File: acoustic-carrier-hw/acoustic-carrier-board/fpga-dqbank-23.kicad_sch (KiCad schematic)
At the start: 0 parts

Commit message: [carrier] Added hierarchical labels
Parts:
- added C15, C5, C58, C59: 10nF, Capacitor_SMD:C_0402_1005Metric, symbol Device:C_Small
- added C17, C18, C33, C36, C49, C57: 0.1uF, Capacitor_SMD:C_0402_1005Metric, symbol Device:C_Small
- added C41: 4.7uF, Capacitor_SMD:C_0402_1005Metric, symbol Device:C_Small
- added C6: 10uF, Capacitor_SMD:C_0603_1608Metric, symbol Device:C_Small
- added IC1: ECP5-BGA256, iw-fpga_mcu:BGA256C80P16X16_1400X1400X170, symbol iw-fpga_mcu:ECP5-BGA256
- added L11: 120@100MHz, Inductor_SMD:L_0603_1608Metric, symbol Device:L_Small
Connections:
- new net CLK: IC1.P15 (PR32B/RDQSN32)
- new net D0: IC1.R16 (PR35B/VREF1_3)
- new net D1: IC1.M13 (PR35C)
- new net D2: IC1.N14 (PR35D/RDQ32)
- new net D3: IC1.N13 (PR38A/RDQ44)
- new net D4: IC1.P14 (PR38B)
- new net D5: IC1.R15 (PR38C)
- new net D6: IC1.T15 (PR38D)
- new net D7: IC1.P13 (PR41A)
- new net DIR: IC1.M14 (PR32D)
- new net DQ0: IC1.B16 (PR2A/RDQ8)
- new net DQ1: IC1.B15 (PR2B/S0_IN)
- new net DQ10: IC1.J12 (PR17D)
- new net DQ11: IC1.J14 (PR20C/GR_PCLK2_1)
- new net DQ12: IC1.K14 (PR20D/GR_PCLK2_0)
- new net DQ13: IC1.J16 (PR23A/PCLKT2_1)
- new net DQ14: IC1.J15 (PR23B/PCLKC2_1)
- new net DQ15: IC1.K16 (PR23C/PCLKT2_0)
- new net DQ2: IC1.C14 (PR2C)
- new net DQ3: IC1.D14 (PR2D)
- new net DQ4: IC1.C16 (PR5A)
- new net DQ5: IC1.C15 (PR5B)
- new net DQ6: IC1.E14 (PR5C)
- new net DQ7: IC1.F14 (PR5D)
- new net DQ8: IC1.H13 (PR17B)
- new net DQ9: IC1.J13 (PR17C)
- new net FPGA_CC1: IC1.R13 (PR41C)
- new net FPGA_CC2: IC1.T14 (PR41D)
- new net FPGA_USB_SENSE: IC1.R12 (PR44A/RDQS44)
- new net GND: C15.2, C17.2, C18.2, C33.2, C36.2, C41.2, C49.2, C5.2, C57.2, C58.2, C59.2, C6.2
- new net LDM: IC1.F13 (PR8C)
- new net LDQS: IC1.D16 (PR8A/RDQS8)
- new net LDQS#: IC1.E15 (PR8B/RDQSN8)
- new net NXT: IC1.P16 (PR35A)
- new net RST: IC1.N16 (PR32A/RDQS32)
- new net STP: IC1.L14 (PR32C)
- new net UDM: IC1.K15 (PR23D/PCLKC2_0/RDQ20)
- new net UDQS: IC1.G16 (PR20A/RDQS20)
- new net UDQS#: IC1.H15 (PR20B/RDQSN20)
- new net VCORE_3V3: C33.1, C36.1, C41.1, IC1.K11 (VCCIO3_1), IC1.L11 (VCCIO3_2)
- new net VDDR3L_1.35: L11.2
- new net VDDR_BANK: C49.1, C57.1, C58.1, C59.1, C6.1, IC1.H11 (VCCIO2_1), IC1.J11 (VCCIO2_2), L11.1
- new net VDRR3L_0.675: C15.1, C17.1, C18.1, C5.1, IC1.G14 (PR14C/VREF1_2)
- no-connect marks 0 -> 25

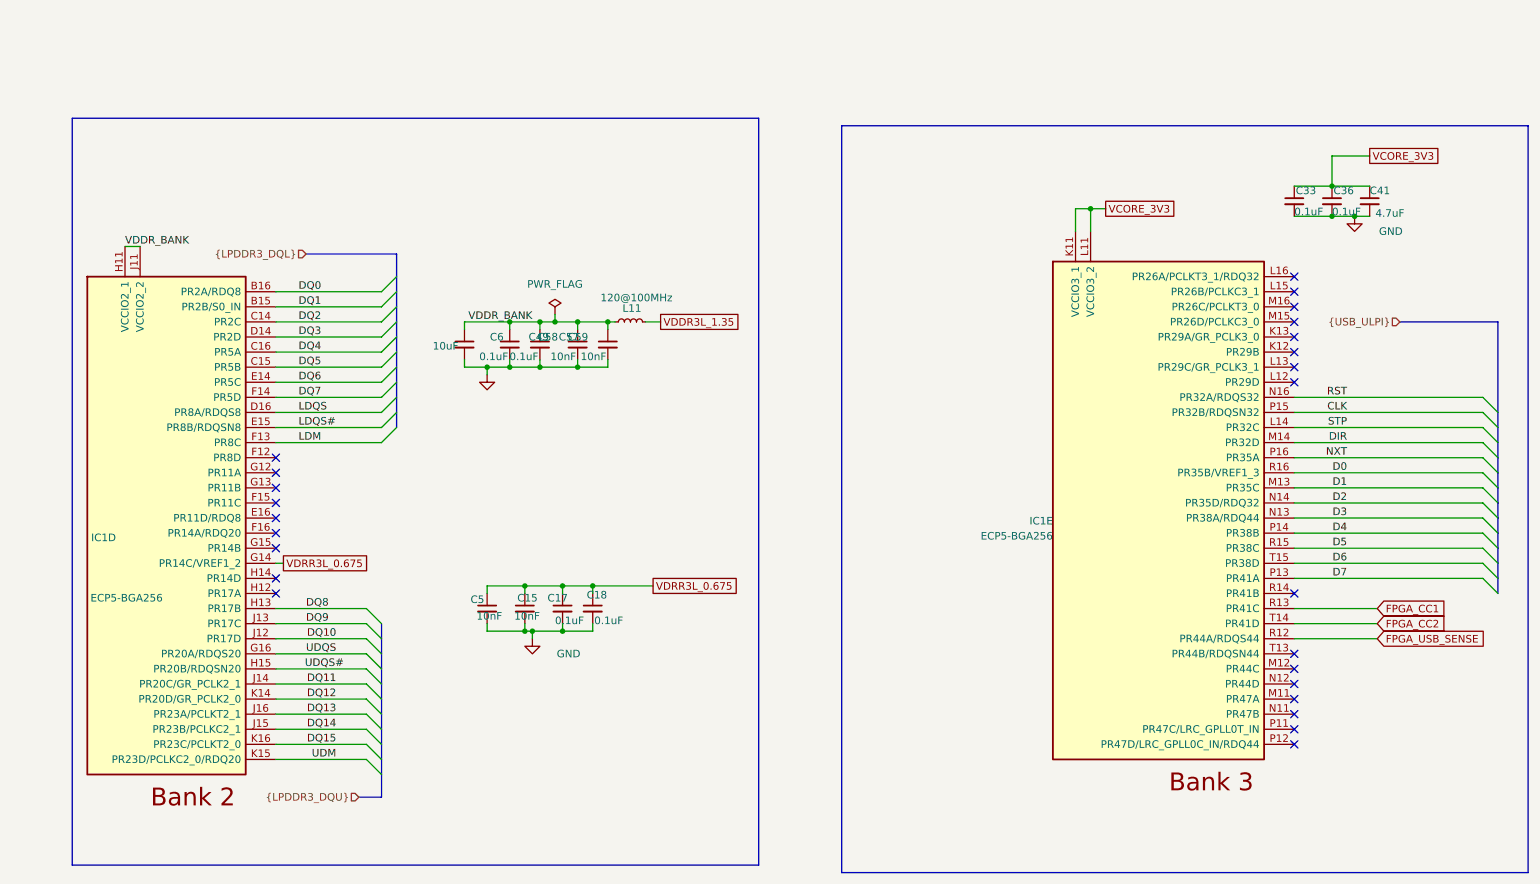
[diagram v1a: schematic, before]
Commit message: [carrier] Added decoupling caps to flash and comparators
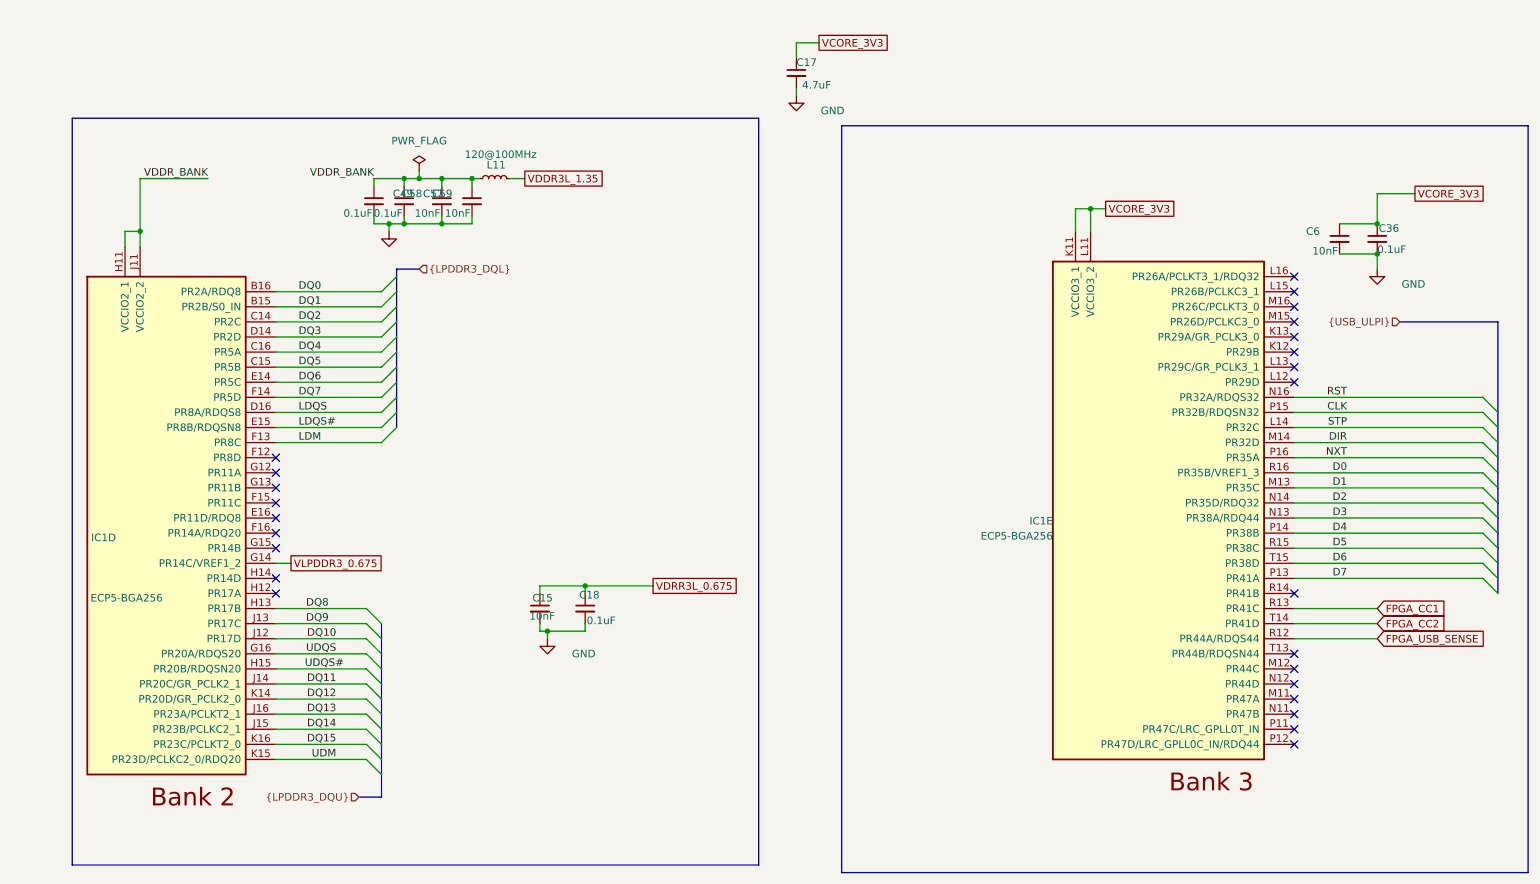
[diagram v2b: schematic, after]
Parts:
- removed C33: 0.1uF, Capacitor_SMD:C_0402_1005Metric, symbol Device:C_Small
- removed C41: 4.7uF, Capacitor_SMD:C_0402_1005Metric, symbol Device:C_Small
- removed C5: 10nF, Capacitor_SMD:C_0402_1005Metric, symbol Device:C_Small
- C17: value 0.1uF -> 4.7uF; LPN C307331 -> C23733; MPN CL05B104KB54PNC -> CL05A475MP5NRNC
- C6: value 10uF -> 10nF; footprint Capacitor_SMD:C_0603_1608Metric -> Capacitor_SMD:C_0402_1005Metric; LPN C19702 -> CL05B103KB5NNNC; MPN CL10A106KP8NNNC -> C15195
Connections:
- net VCORE_3V3: now also C17.1, C6.1
- net VDDR_BANK: no longer C6.1
- net VDRR3L_0.675: no longer C17.1, IC1.G14 (PR14C/VREF1_2)
- new net VLPDDR3_0.675: IC1.G14 (PR14C/VREF1_2)
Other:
- moved on the sheet: C15, C18, C36, C49, C57, C58, C59, L11

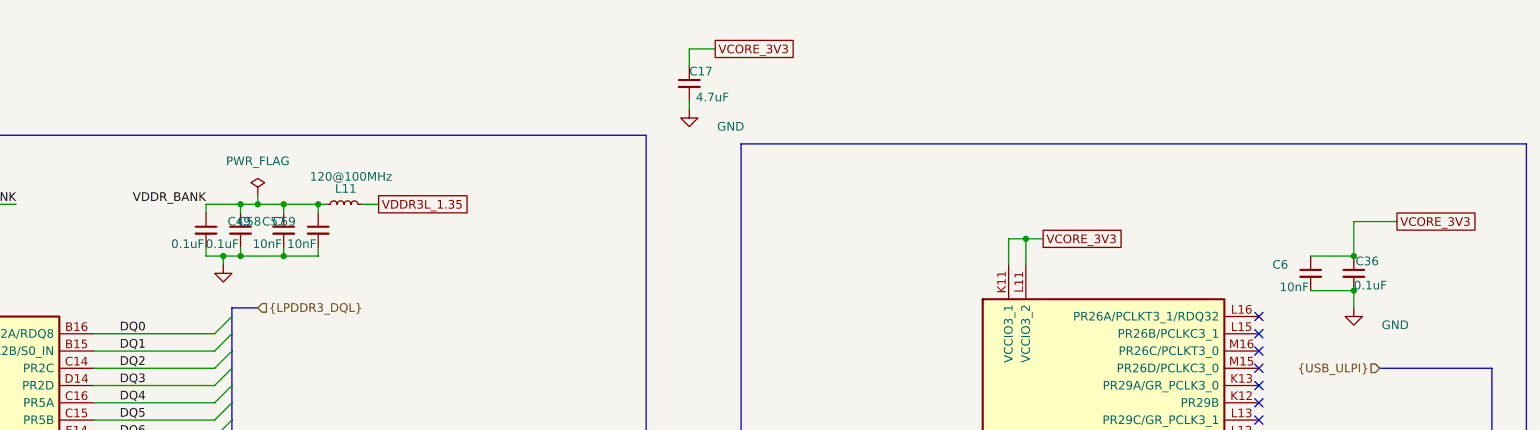
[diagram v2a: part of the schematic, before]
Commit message: [carrier] Added extra decoupling to ECP5U according to datasheet (next) perform page-wise checks, add testpoints
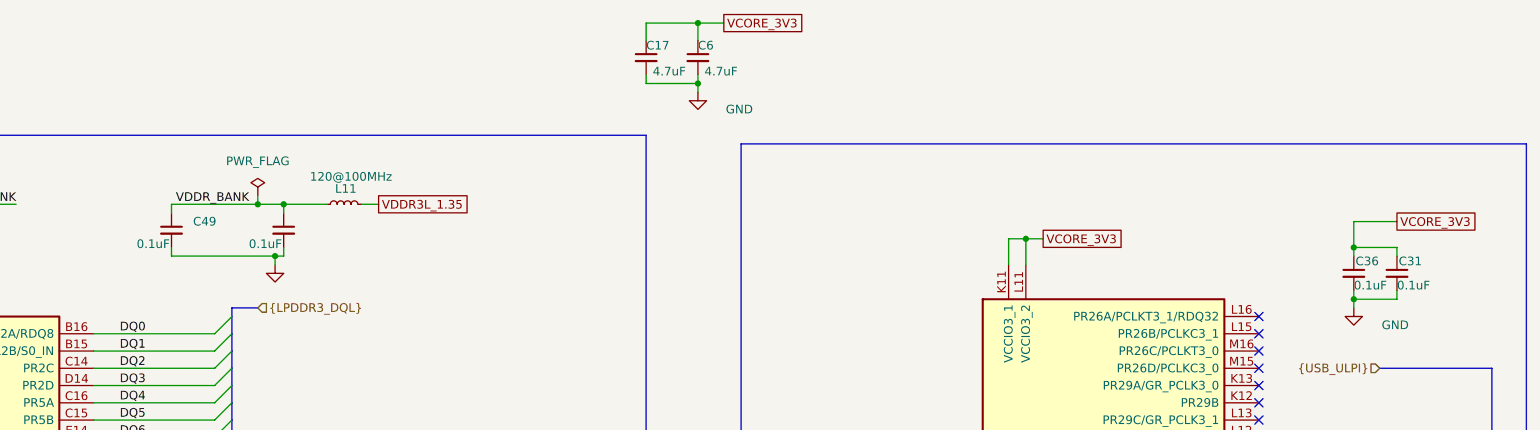
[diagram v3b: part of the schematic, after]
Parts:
- removed C58, C59: 10nF, Capacitor_SMD:C_0402_1005Metric, symbol Device:C_Small
- added C31: 0.1uF, Capacitor_SMD:C_0402_1005Metric, symbol Device:C_Small
- C6: value 10nF -> 4.7uF; LPN CL05B103KB5NNNC -> C23733; MPN C15195 -> CL05A475MP5NRNC
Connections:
- net GND: now also C31.2
- net VCORE_3V3: now also C31.1
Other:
- moved on the sheet: C49

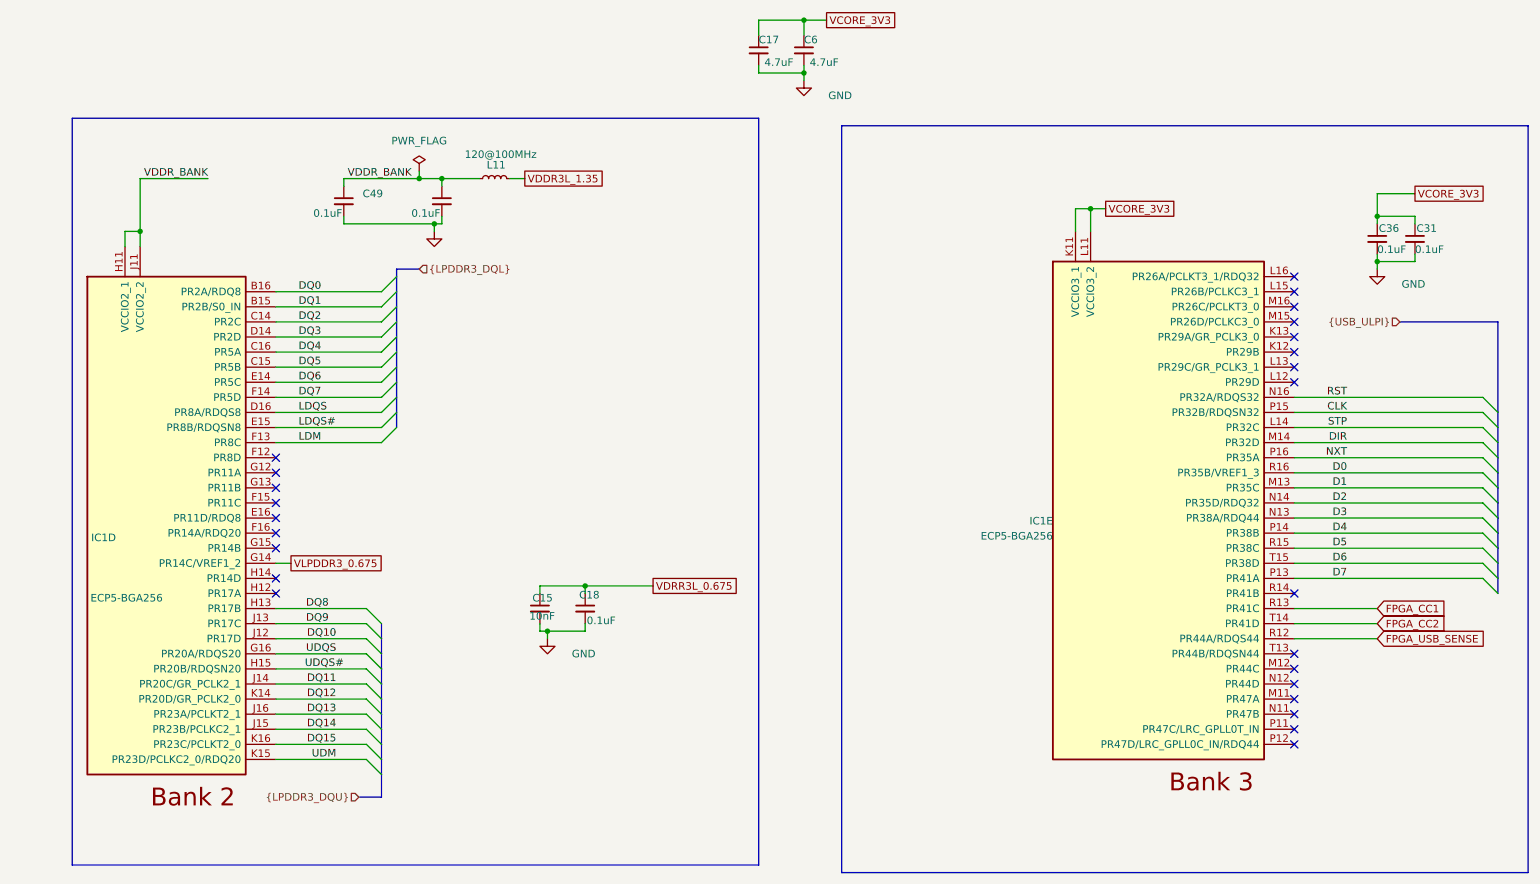
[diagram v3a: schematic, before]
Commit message: [¢arrier] Did major cchecks of ETH, DDR, ANALOG, config (next) check buffer circuit driven by USB-CC, then start layout
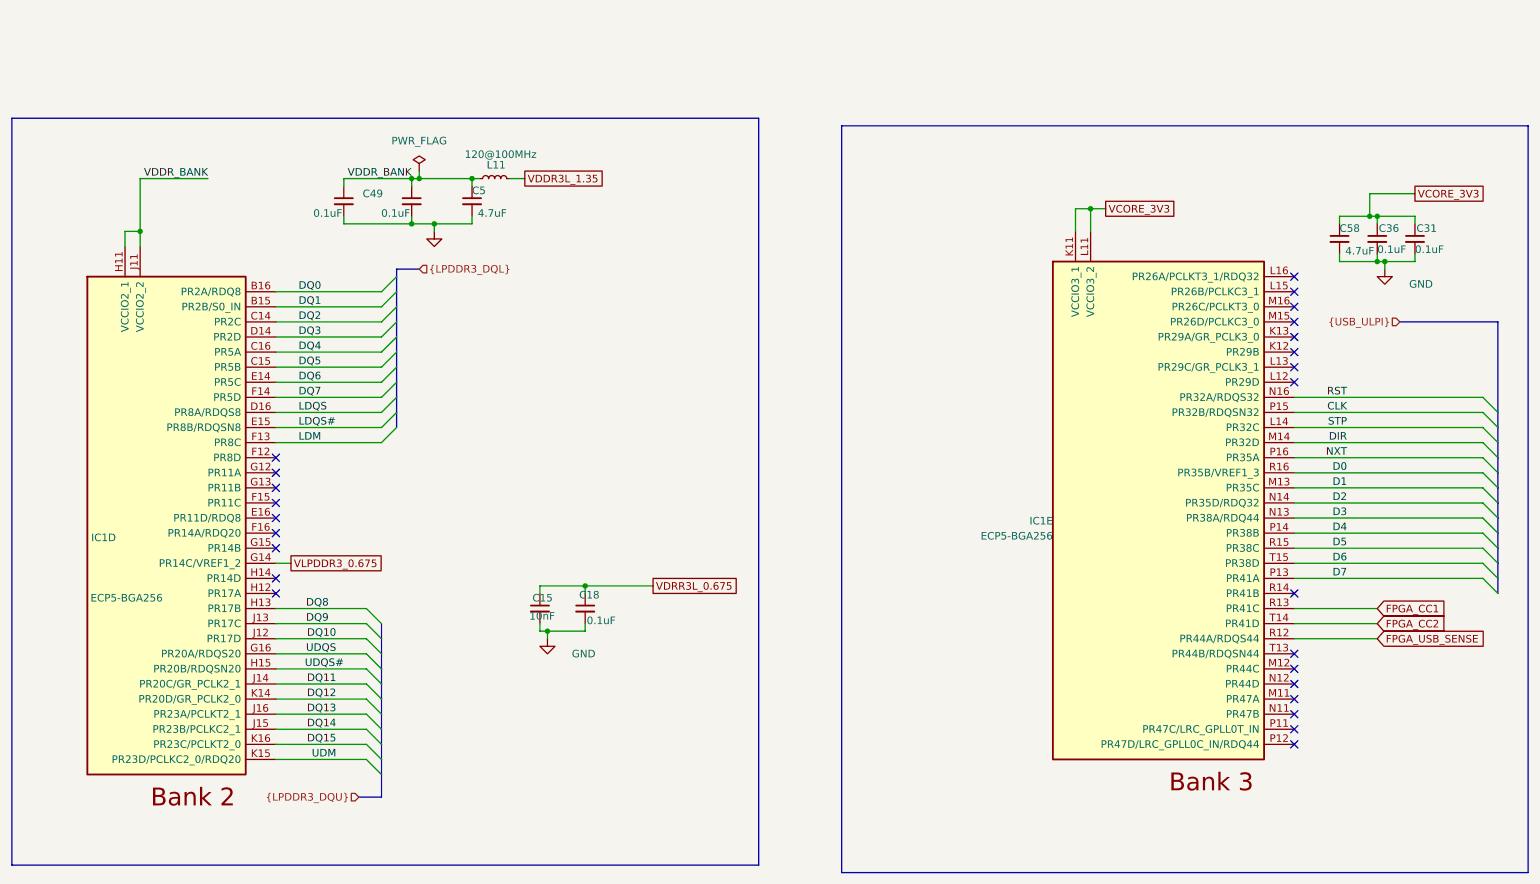
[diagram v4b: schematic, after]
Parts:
- removed C17, C6: 4.7uF, Capacitor_SMD:C_0402_1005Metric, symbol Device:C_Small
- added C5, C58: 4.7uF, Capacitor_SMD:C_0402_1005Metric, symbol Device:C_Small
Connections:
- net GND: now also C5.2, C58.2
- net VCORE_3V3: now also C58.1
- net VDDR_BANK: now also C5.1

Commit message: [carrier] Did some check for example schematics, starting layout
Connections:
- net CLK: now also IC1.K13 (PR29A/GR_PCLK3_0); no longer IC1.P15 (PR32B/RDQSN32)
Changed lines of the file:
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@@
-	)
-	(no_connect
-		(at 242.57 69.85)
 	)
 	(no_connect
@@
 	)
 	(no_connect
+		(at 242.57 82.55)
+	)
+	(no_connect
 		(at 71.12 92.71)
 	)
@@
 	)
 	(bus_entry
-		(at 274.32 82.55)
-		(size 2.54 2.54)
-		(stroke
-			(width 0)
-			(type default)
-		)
-	)
-	(bus_entry
 		(at 88.9 130.81)
 		(size -2.54 -2.54)
@@
 	)
 	(bus_entry
+		(at 274.32 69.85)
+		(size 2.54 2.54)
+		(stroke
+			(width 0)
+			(type default)
+		)
+	)
+	(bus_entry
 		(at 274.32 102.87)
 		(size 2.54 2.54)
@@
 	(wire
 		(pts
-			(xy 242.57 82.55) (xy 274.32 82.55)
-		)
-		(stroke
-			(width 0)
-			(type default)
-		)
-	)
-	(wire
-		(pts
 			(xy 205.74 48.26) (xy 208.28 48.26)
 		)
@@
 		)
 	)
+	(wire
+		(pts
+			(xy 242.57 69.85) (xy 274.32 69.85)
+		)
+		(stroke
+			(width 0)
+			(type default)
+		)
+	)
 	(bus
 		(pts
@@
 		)
 	)
-	(bus
-		(pts
-			(xy 276.86 85.09) (xy 276.86 87.63)
-		)
-		(stroke
-			(width 0)
-			(type default)
-		)
-	)
 	(wire
 		(pts
@@
 	(bus
 		(pts
-			(xy 276.86 82.55) (xy 276.86 85.09)
+			(xy 276.86 82.55) (xy 276.86 87.63)
 		)
 		(stroke
@@
 		)
 	)
+	(bus
+		(pts
+			(xy 276.86 72.39) (xy 276.86 82.55)
+		)
+		(stroke
+			(width 0)
+			(type default)
+		)
+	)
 	(wire
 		(pts
@@
 	(bus
 		(pts
-			(xy 276.86 67.31) (xy 276.86 82.55)
+			(xy 276.86 67.31) (xy 276.86 72.39)
 		)
 		(stroke
@@
 		)
 	)
+	(label "CLK"
+		(at 251.46 69.85 180)
+		(effects
+			(font
+				(size 1.27 1.27)
+			)
+			(justify right bottom)
+		)
+	)
 	(label "DQ15"
 		(at 81.28 138.43 180)
@@
 		)
 	)
-	(label "CLK"
-		(at 251.46 82.55 180)
-		(effects
-			(font
-				(size 1.27 1.27)
-			)
-			(justify right bottom)
-		)
-	)
